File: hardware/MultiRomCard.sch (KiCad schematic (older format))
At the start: 29 parts, among them P1 VC4000_Cartridge_Bus, P2 MicroSD_Breakout, P3 DISPLAY, SW1 UP, SW2 DOWN, SW3 SELECT, U1 Arduino_Nano, U10 74HC32, U2 74HC595, U3 74HC595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

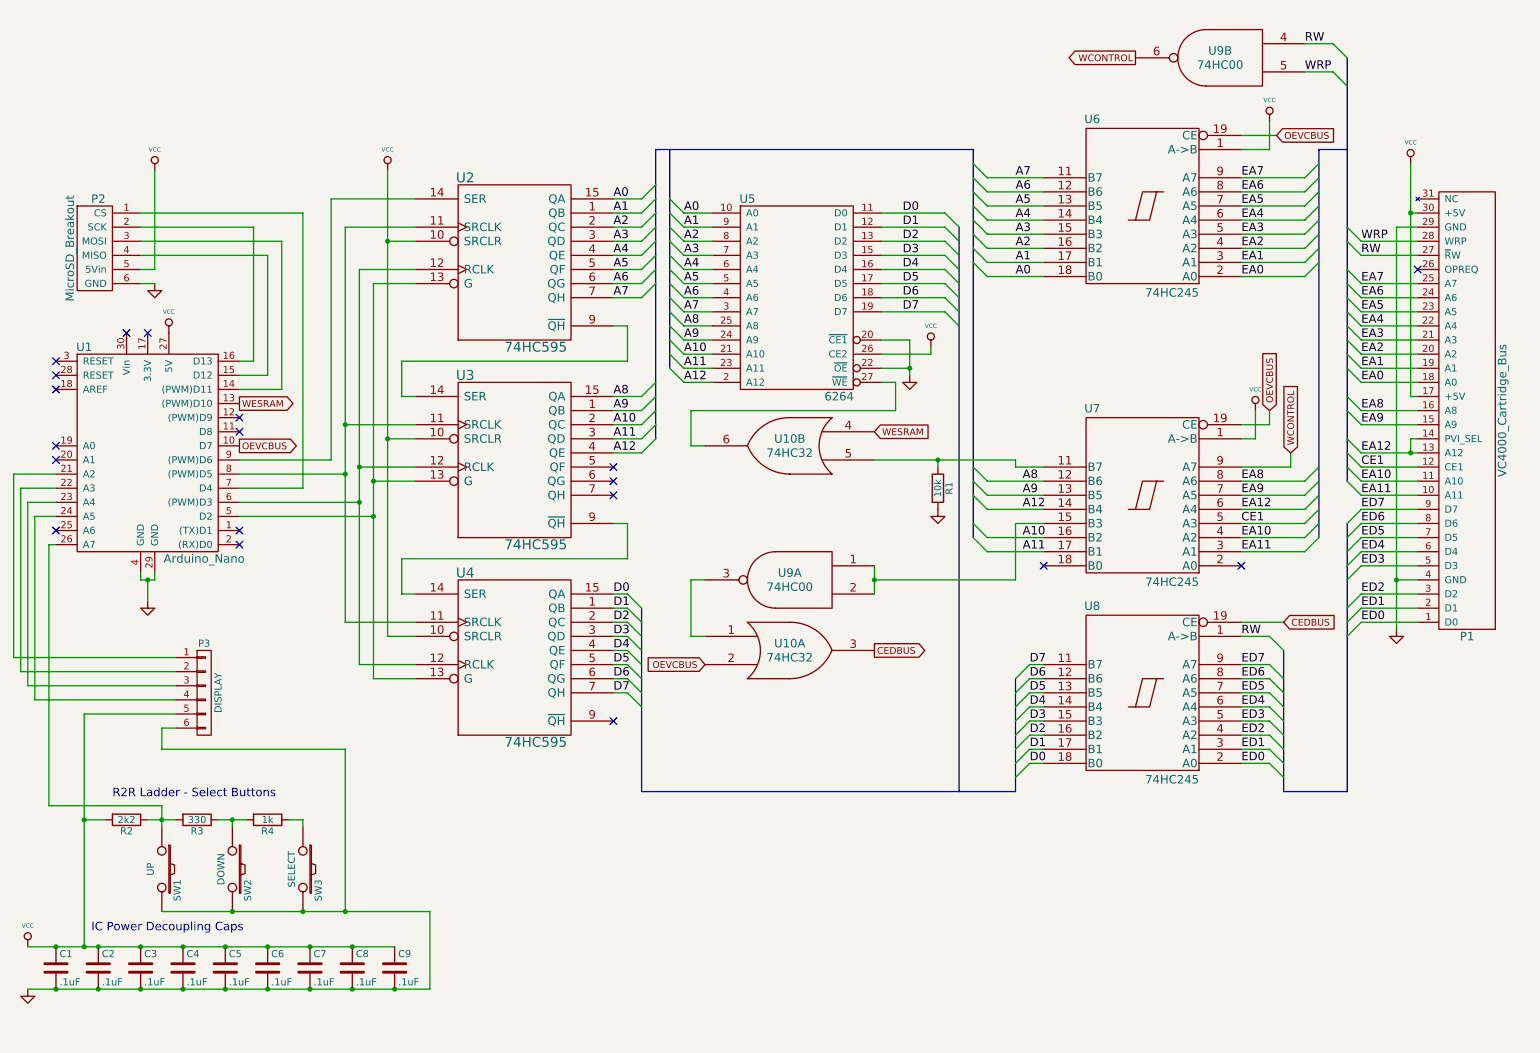
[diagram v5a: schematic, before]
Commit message: clean up of schema for additional components
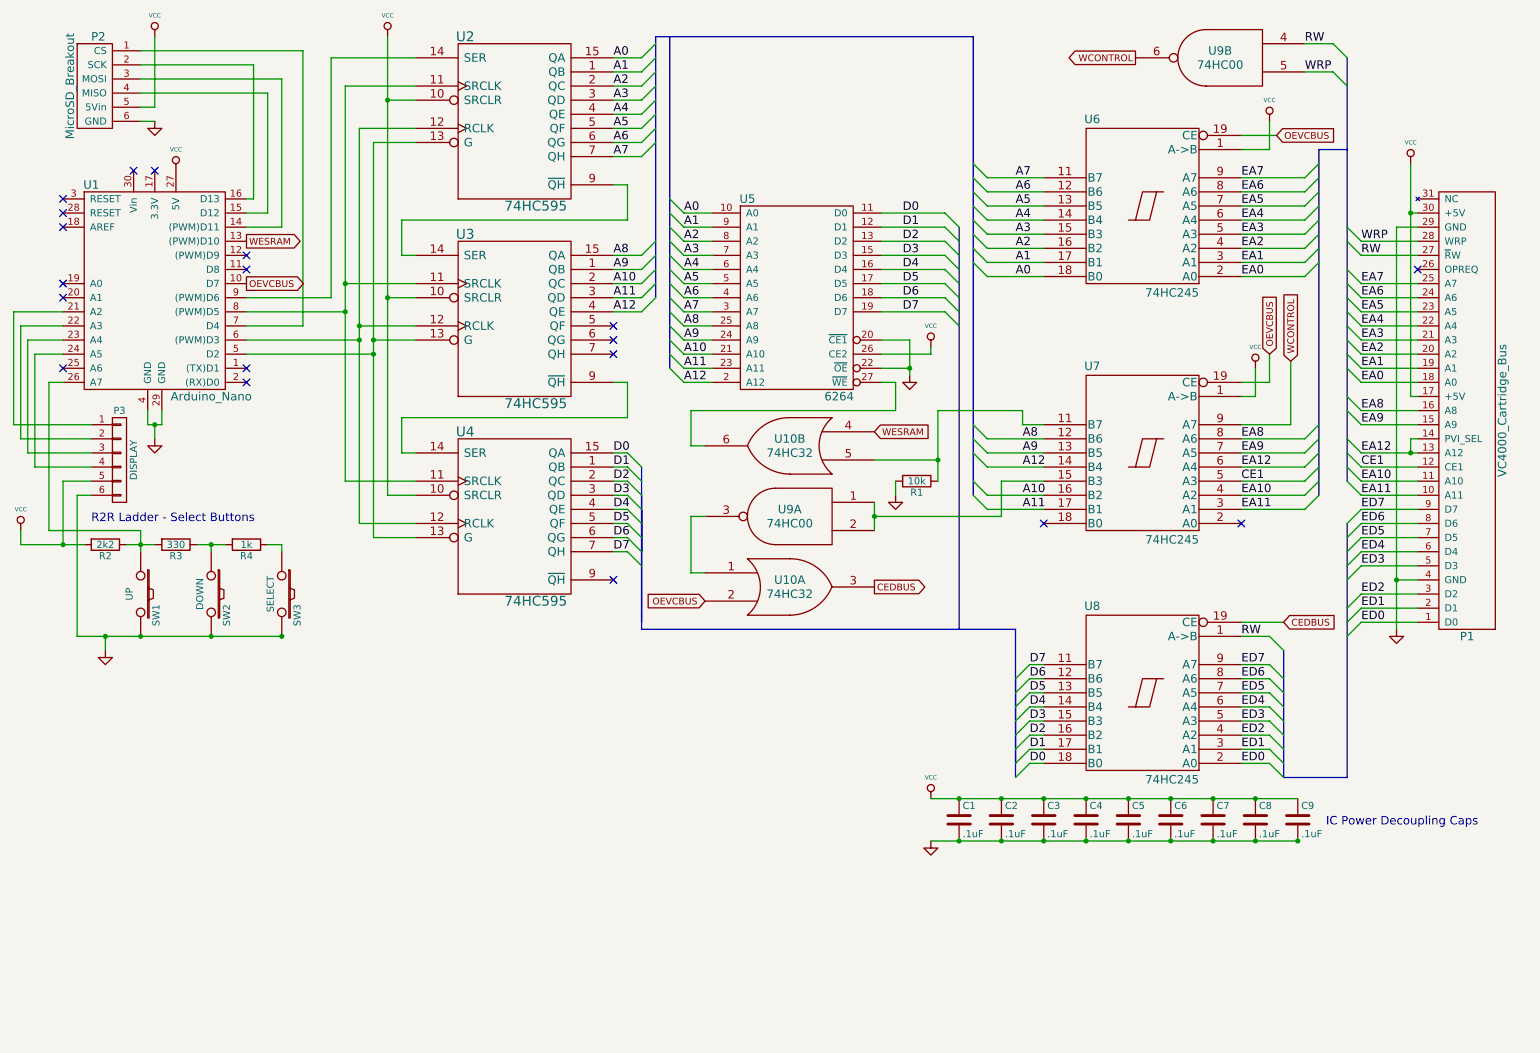
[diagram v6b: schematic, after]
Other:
- moved on the sheet: C1, C2, C3, C4, C5, C6, C7, C8, C9, P2, P3, R1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

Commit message: added 2x 7-segment displays and shift register for display
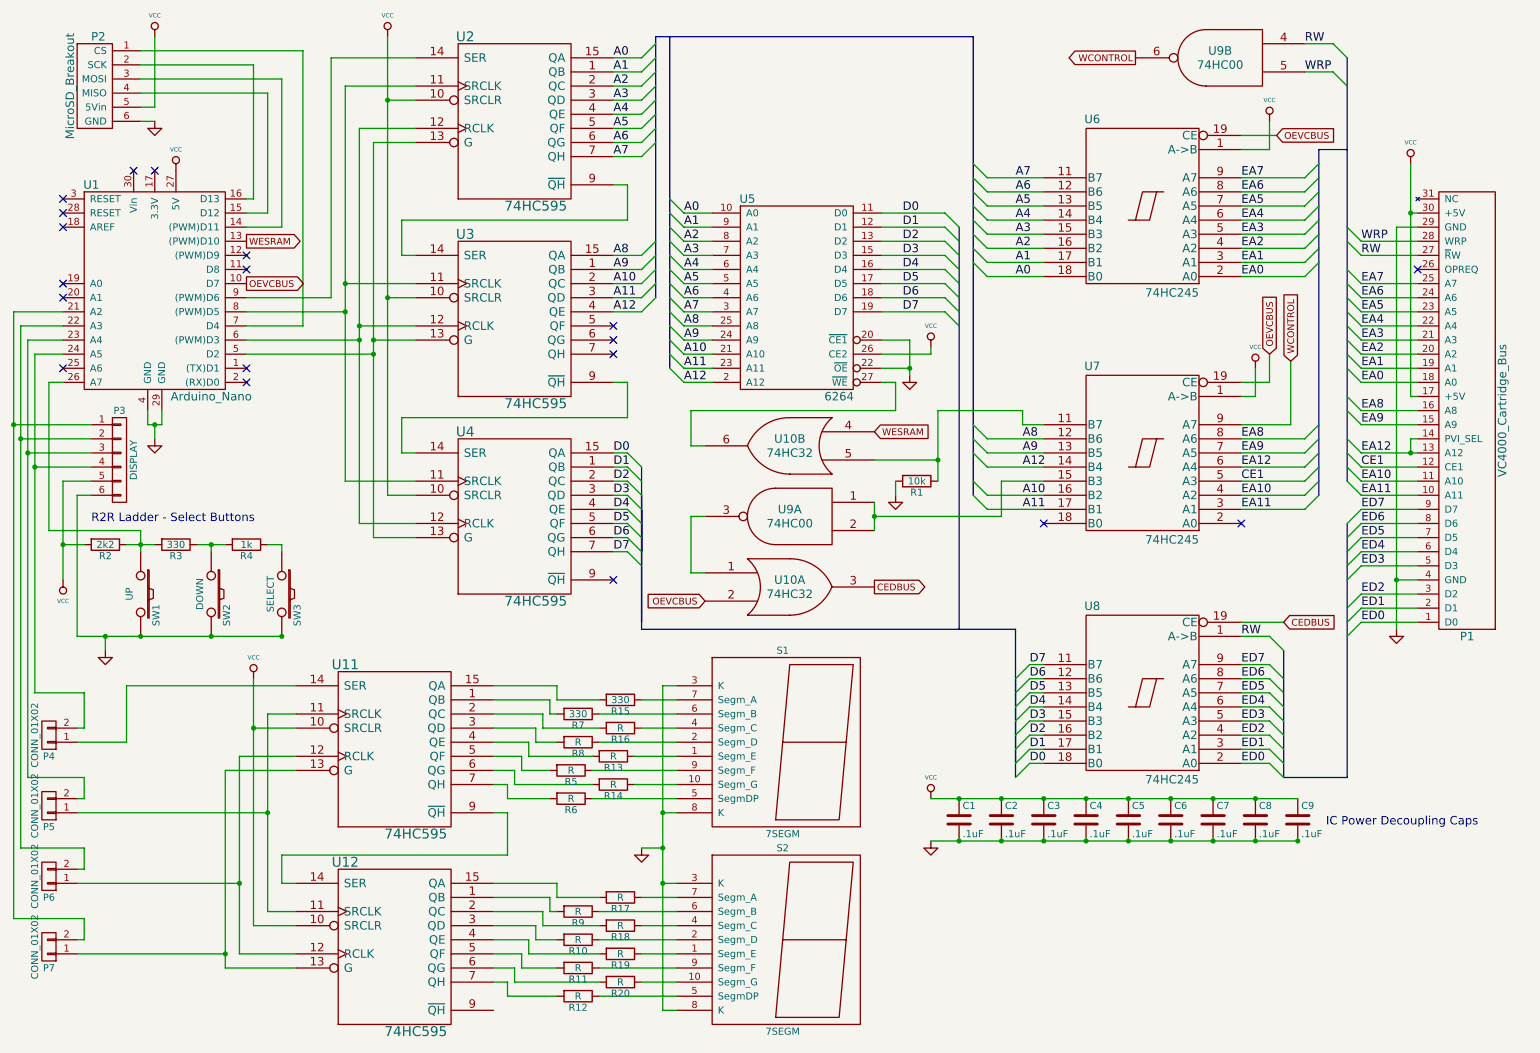
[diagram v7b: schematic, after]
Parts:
- added P4, P5, P6, P7: CONN_01X02, symbol CONN_01X02
- added R10, R11, R12, R13, R14, R16, R17, R18, R19, R20, R5, R6, R8, R9: R, symbol R
- added R15, R7: 330, symbol R
- added S1, S2: 7SEGM, symbol 7SEGM
- added U11, U12: 74HC595, Housings_DIP:DIP-16_W7.62mm_LongPads, symbol 74HC595
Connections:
- net GND: now also S1.3 (K), S1.8 (K), S2.3 (K), S2.8 (K), U11.8 (GND), U12.8 (GND)
- net VCC: now also U11.10 (SRCLR), U11.16 (VCC), U12.10 (SRCLR), U12.16 (VCC)
- net at P3.1 (P1), U1.21 (A2): now also P7.2 (P2)
- net at P3.2 (P2), U1.22 (A3): now also P6.2 (P2)
- net at P3.3 (P3), U1.23 (A4): now also P5.2 (P2)
- net at P3.4 (P4), U1.24 (A5): now also P4.2 (P2)
- new net: R19.1, S2.1 (Segm_E)
- new net: R20.1, S2.10 (Segm_G)
- new net: R10.1, S2.2 (Segm_D)
- new net: R18.1, S2.4 (Segm_C)
- new net: R12.1, S2.5 (SegmDP)
- new net: R9.1, S2.6 (Segm_B)
- new net: R17.1, S2.7 (Segm_A)
- new net: R11.1, S2.9 (Segm_F)
- new net: R13.1, S1.1 (Segm_E)
- new net: R14.1, S1.10 (Segm_G)
- new net: R8.1, S1.2 (Segm_D)
- new net: R16.1, S1.4 (Segm_C)
- new net: R6.1, S1.5 (SegmDP)
- new net: R7.1, S1.6 (Segm_B)
- new net: R15.1, S1.7 (Segm_A)
- new net: R5.1, S1.9 (Segm_F)
- new net: R7.2, U11.1 (QB)
- new net: P5.1 (P1), U11.11 (SRCLK), U12.11 (SRCLK)
- new net: P6.1 (P1), U11.12 (RCLK), U12.12 (RCLK)
- new net: P7.1 (P1), U11.13 (G), U12.13 (G)
- new net: P4.1 (P1), U11.14 (SER)
- new net: R15.2, U11.15 (QA)
- new net: R16.2, U11.2 (QC)
- new net: R8.2, U11.3 (QD)
- new net: R13.2, U11.4 (QE)
- new net: R5.2, U11.5 (QF)
- new net: R14.2, U11.6 (QG)
- new net: R6.2, U11.7 (QH)
- new net: U11.9 (~QH), U12.14 (SER)
- new net: R9.2, U12.1 (QB)
- new net: R17.2, U12.15 (QA)
- new net: R18.2, U12.2 (QC)
- new net: R10.2, U12.3 (QD)
- new net: R19.2, U12.4 (QE)
- new net: R11.2, U12.5 (QF)
- new net: R20.2, U12.6 (QG)
- new net: R12.2, U12.7 (QH)

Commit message: [HW] Update PCB to v. 0.3 (include 7-segm display).
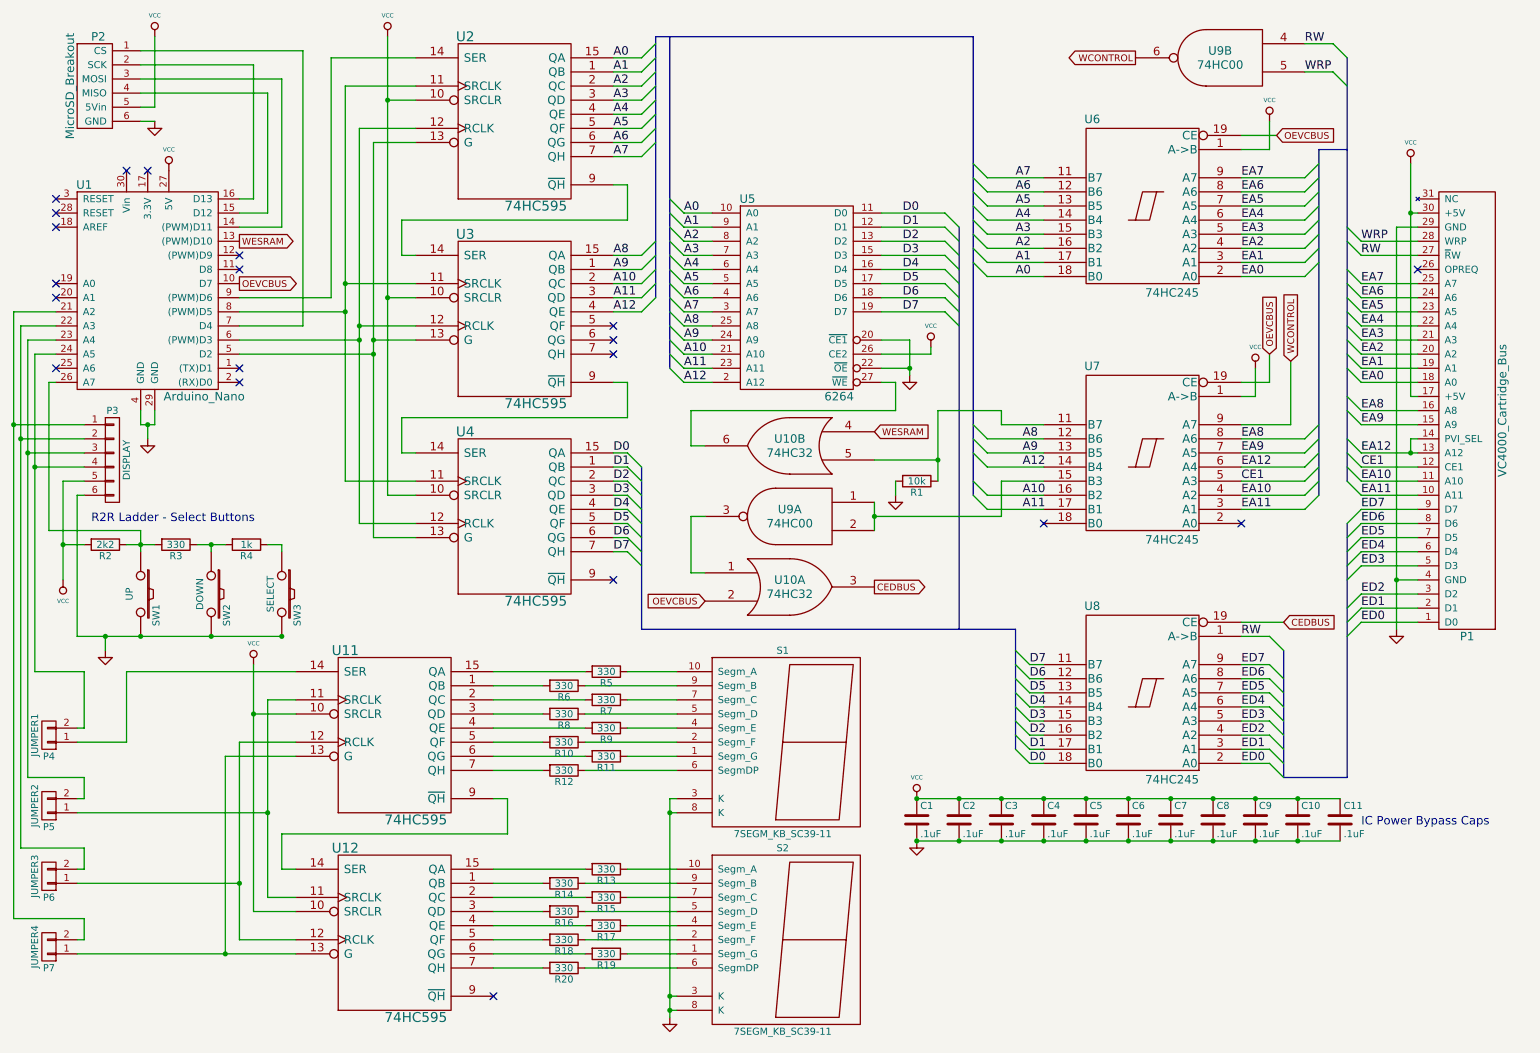
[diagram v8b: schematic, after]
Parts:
- removed S1, S2: 7SEGM, symbol 7SEGM
- added C10, C11: .1uF, Capacitors_ThroughHole:C_Rect_L7_W2_P5, symbol C
- added S1, S2: 7SEGM_KB_SC39-11, VC4000_MultiRom:7_Segment_Display_KB_13_10mm, symbol 7SEGM_KB_SC39-11
- C1, C2, C3, C4, C5, C6, C7, C8, C9: footprint Capacitors_ThroughHole:C_Disc_D6_P5 -> Capacitors_ThroughHole:C_Rect_L7_W2_P5
- P4: value CONN_01X02 -> JUMPER1; footprint (none) -> Pin_Headers:Pin_Header_Straight_1x02
- P5: value CONN_01X02 -> JUMPER2; footprint (none) -> Pin_Headers:Pin_Header_Straight_1x02
- P6: value CONN_01X02 -> JUMPER3; footprint (none) -> Pin_Headers:Pin_Header_Straight_1x02
- P7: value CONN_01X02 -> JUMPER4; footprint (none) -> Pin_Headers:Pin_Header_Straight_1x02
- R10: renamed from R5; value R -> 330; footprint (none) -> Resistors_ThroughHole:Resistor_Horizontal_RM10mm
- R11: renamed from R14; value R -> 330; footprint (none) -> Resistors_ThroughHole:Resistor_Horizontal_RM10mm
- R12: renamed from R6; value R -> 330; footprint (none) -> Resistors_ThroughHole:Resistor_Horizontal_RM10mm
- R13: renamed from R17; value R -> 330; footprint (none) -> Resistors_ThroughHole:Resistor_Horizontal_RM10mm
- R14: renamed from R9; value R -> 330; footprint (none) -> Resistors_ThroughHole:Resistor_Horizontal_RM10mm
- R15: renamed from R18; value R -> 330; footprint (none) -> Resistors_ThroughHole:Resistor_Horizontal_RM10mm
- R16: renamed from R10; value R -> 330; footprint (none) -> Resistors_ThroughHole:Resistor_Horizontal_RM10mm
- R17: renamed from R19; value R -> 330; footprint (none) -> Resistors_ThroughHole:Resistor_Horizontal_RM10mm
- R18: renamed from R11; value R -> 330; footprint (none) -> Resistors_ThroughHole:Resistor_Horizontal_RM10mm
- R19: renamed from R20; value R -> 330; footprint (none) -> Resistors_ThroughHole:Resistor_Horizontal_RM10mm
- R20: renamed from R12; value R -> 330; footprint (none) -> Resistors_ThroughHole:Resistor_Horizontal_RM10mm
- R5: renamed from R15; footprint (none) -> Resistors_ThroughHole:Resistor_Horizontal_RM10mm
- R6: renamed from R7; footprint (none) -> Resistors_ThroughHole:Resistor_Horizontal_RM10mm
- R7: renamed from R16; value R -> 330; footprint (none) -> Resistors_ThroughHole:Resistor_Horizontal_RM10mm
- R8: value R -> 330; footprint (none) -> Resistors_ThroughHole:Resistor_Horizontal_RM10mm
- R9: renamed from R13; value R -> 330; footprint (none) -> Resistors_ThroughHole:Resistor_Horizontal_RM10mm
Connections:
- net GND: now also C10.2, C11.2, S1.3 (K), S1.8 (K), S2.3 (K), S2.8 (K)
- net VCC: now also C10.1, C11.1
- net at R17.1: now also S2.4 (Segm_E)
- net at R19.1: now also S2.1 (Segm_G)
- net at R16.1: now also S2.5 (Segm_D)
- net at R15.1: now also S2.7 (Segm_C)
- net at R20.1: now also S2.6 (SegmDP)
- net at R14.1: now also S2.9 (Segm_B)
- net at R13.1: now also S2.10 (Segm_A)
- net at R18.1: now also S2.2 (Segm_F)
- net at R9.1: now also S1.4 (Segm_E)
- net at R11.1: now also S1.1 (Segm_G)
- net at R8.1: now also S1.5 (Segm_D)
- net at R7.1: now also S1.7 (Segm_C)
- net at R12.1: now also S1.6 (SegmDP)
- net at R6.1: now also S1.9 (Segm_B)
- net at R5.1: now also S1.10 (Segm_A)
- net at R10.1: now also S1.2 (Segm_F)
- no-connect marks 19 -> 20
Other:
- note added: "IC Power Bypass Caps"
- note removed: "IC Power Decoupling Caps"
- moved on the sheet: C1, C2, C3, C4, C5, C6, C7, C8, C9, P3, R10, R11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
